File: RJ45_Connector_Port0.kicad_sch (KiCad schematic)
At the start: 13 parts, among them J1 0826-1X4T-43-F

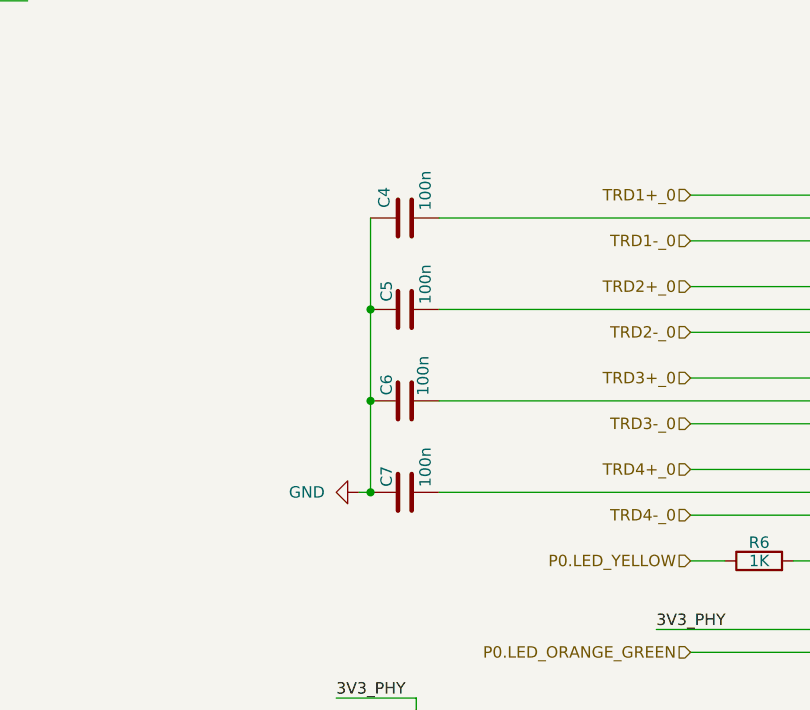
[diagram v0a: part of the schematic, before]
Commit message: updates symbols and fixes ERC errors. Refs: #9
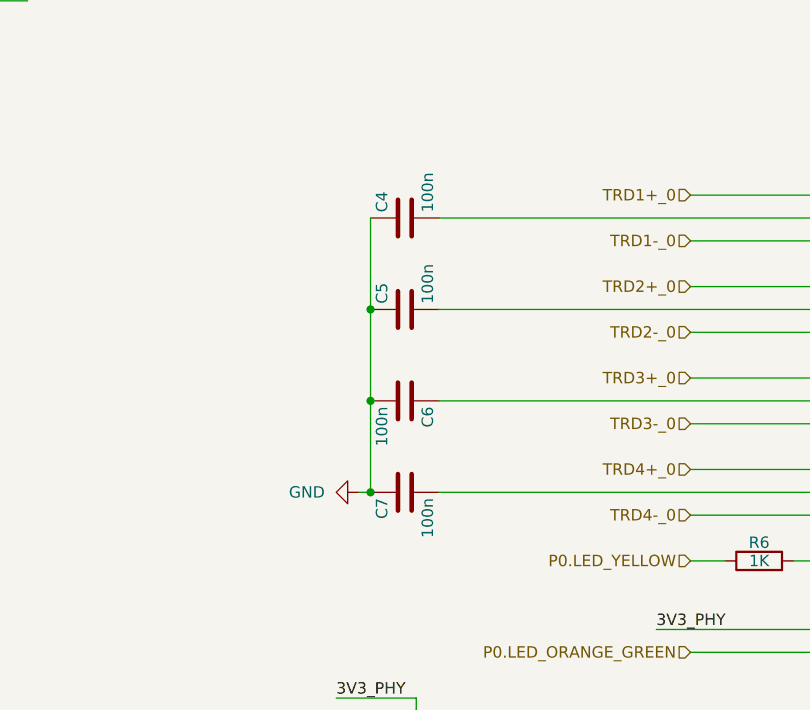
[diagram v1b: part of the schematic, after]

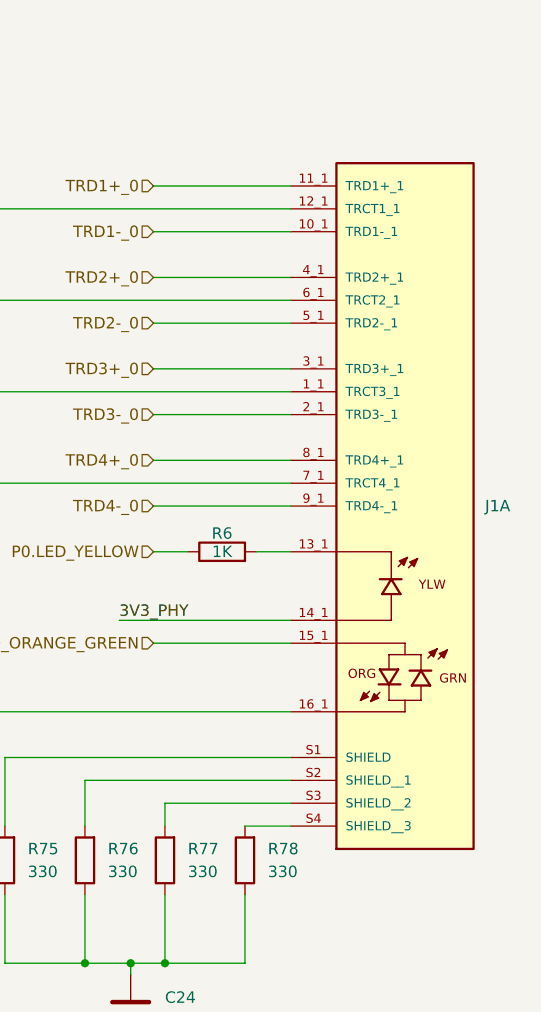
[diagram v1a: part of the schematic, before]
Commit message: updates components to latest library. Refs: #30
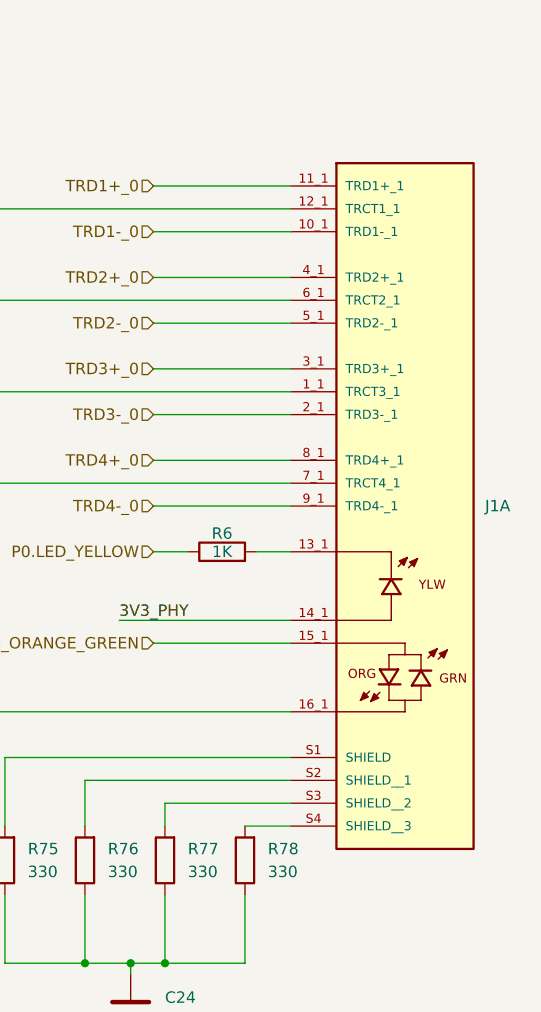
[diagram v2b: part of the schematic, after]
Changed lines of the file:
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@@
 			)
 		)
-		(property "Datasheet" ""
+		(property "Datasheet" "https://www.belfuse.com/media/drawings/products/magjack%20ICMs/dr-mag-0826-1x4t-43-f.pdf"
 			(at 139.7 69.85 0)
 			(effects

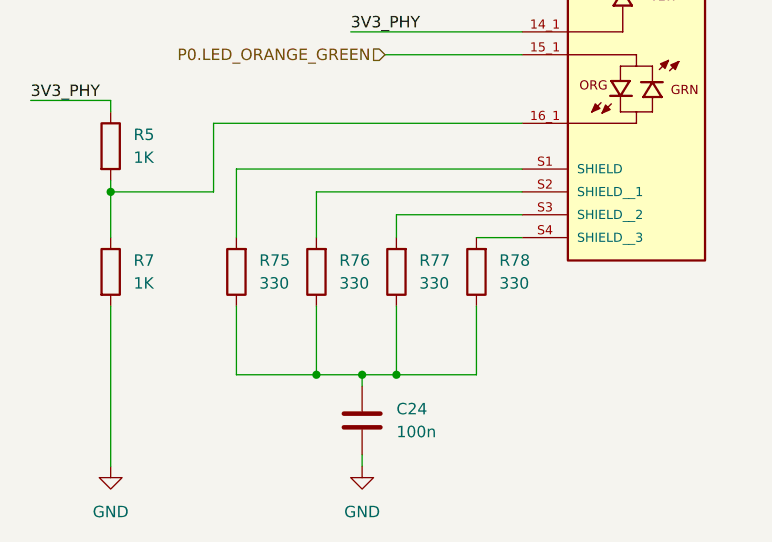
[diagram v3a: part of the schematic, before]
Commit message: updates RJ45_Connector_Port0. Refs: #41
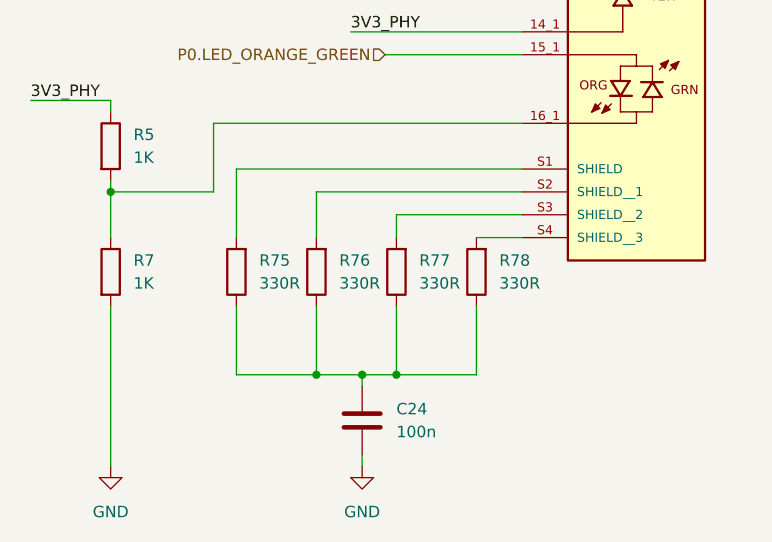
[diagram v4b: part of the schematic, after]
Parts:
- C24, C4, C5, C6, C7: symbol KL_C:C_100n_50V_X7R_0603_10 -> KL_C:C_100n_50V_10pct_X7R_0603; Dielectric (none) -> X7R; MPN (none) -> CL10B104KB8NNNC; Package_in_inch (none) -> 0603; Tolerance 20 -> (none); Tolerance_in_pct (none) -> 10; Voltage 10 -> (none); Voltage_in_V (none) -> 50
- J1: value 0826-1X4T-43-F -> RJ45_0826-1X4T-43-F; symbol KL_Connectors_RJ45:0826-1X4T-43-F -> KL_Conn_Data:RJ45_0826-1X4T-43-F; MANUFACTURER Bel Fuse -> (none); MAXIMUM_PACKAGE_HEIGHT 15.49mm -> (none); MPN (none) -> 0826-1X4T-43-F; PARTREV D -> (none); STANDARD Manufacturer Recommendations -> (none)
- R5, R6, R7: symbol KL_R:R_1K_100mW_5_0603 -> KL_R:R_1K_0.1W_5pct_0603; MPN (none) -> CRGCQ0603J1K0; Package (in) 0603 -> (none); Package_in_inch (none) -> 0603; Power 100mW -> (none); Power_in_W (none) -> 0.1; Tolerance 5 -> (none); Tolerance_in_pct (none) -> 5
- R75, R76, R77, R78: value 330 -> 330R; symbol KL_R:R_330R_100mW_1_0603 -> KL_R:R_330R_0.1W_1pct_0603; Farnell 9238425RL -> (none); MPN (none) -> RC0603FR-07330RL; Package (in) 0603 -> (none); Package_in_inch (none) -> 0603; Power 100mW -> (none); Power_in_W (none) -> 0.1; Tolerance 1% -> (none); Tolerance_in_pct (none) -> 1
